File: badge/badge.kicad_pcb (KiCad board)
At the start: 2 copper layers, 39.4 x 73 mm, 13 parts, among them K1 KEYSW, K2 KEYSW, K3 KEYSW, K4 KEYSW, U1 ProMicro

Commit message: Move logos around a bit
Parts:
- moved G*** 1.42 mm to (130.8, 55.2)
- moved G*** 0.64 mm to (130.8, 26.0)
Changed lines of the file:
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@@
   )
   (module components:rose (layer B.Cu)
-    (at 130.175 53.975)
+    (at 130.81 55.245)
     (fp_text reference G*** (at 0 0) (layer B.SilkS) hide
       (effects (font (size 1.524 1.524) (thickness 0.3)) (justify mirror))
@@
   )
   (module components:pdxkbc (layer F.Cu)
-    (at 130.81 25.4)
+    (at 130.81 26.035)
     (fp_text reference G*** (at 0 0) (layer F.SilkS) hide
       (effects (font (size 1.524 1.524) (thickness 0.3)))
@@
   (gr_line (start 147.955 20.32) (end 112.395 20.32) (layer Edge.Cuts) (width 0.15))
   (gr_arc (start 112.395 22.225) (end 112.395 20.32) (angle -90) (layer Edge.Cuts) (width 0.15))
-  (gr_text "@fharding0\n" (at 130.175 22.225) (layer B.Mask)
+  (gr_text "@fharding0\n" (at 130.175 22.86) (layer B.Mask)
     (effects (font (size 1.5 1.5) (thickness 0.3)) (justify mirror))
   )

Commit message: Make rose smaller so it doesn't expose nodes
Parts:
- moved G*** 4.45 mm to (130.8, 50.8)

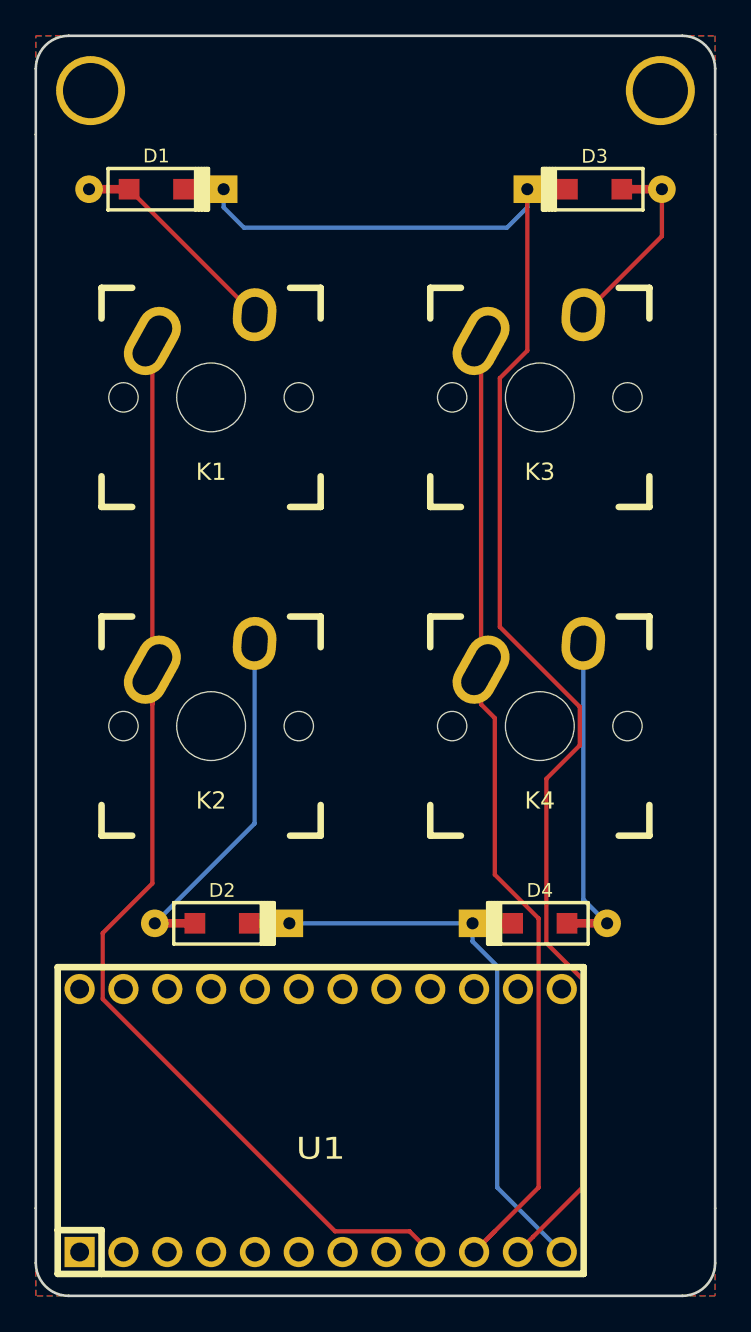
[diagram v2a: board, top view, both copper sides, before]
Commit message: Cleanup routing, position logos relatively
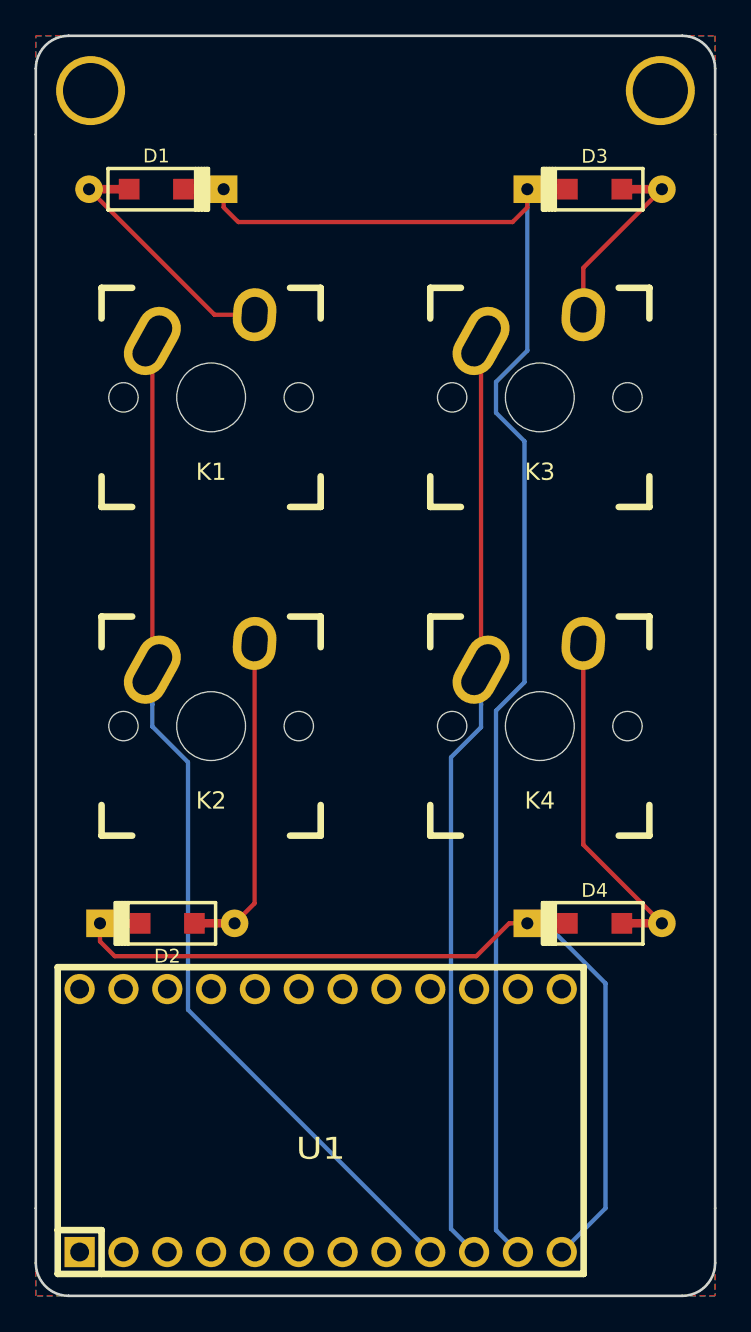
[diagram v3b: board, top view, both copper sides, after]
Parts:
- moved G*** 20.8 mm to (130.3, 30.0), turned to 8 degrees
- moved D4 3.18 mm to (142.9, 71.8)
- moved D2 3.17 mm to (118.1, 71.8), turned to 0 degrees
- moved G*** 0.96 mm to (130.2, 25.3)
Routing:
- net /row1: track 31.8 -> 49.6 mm
- net /col0: track 66.4 -> 59.5 mm
- net /row0: track 88.1 -> 84.6 mm
- net /col1: track 57.4 -> 54.1 mm
- net Net-(D2-Pad2): track 18.6 -> 16.7 mm
- net Net-(D4-Pad2): track 16.8 -> 18.1 mm
- net Net-(D1-Pad2): track 13.5 -> 12.6 mm
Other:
- board text added: "rev v2.0"
